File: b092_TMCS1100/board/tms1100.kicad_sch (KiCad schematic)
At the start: 5 parts, among them U1 TMCS1100

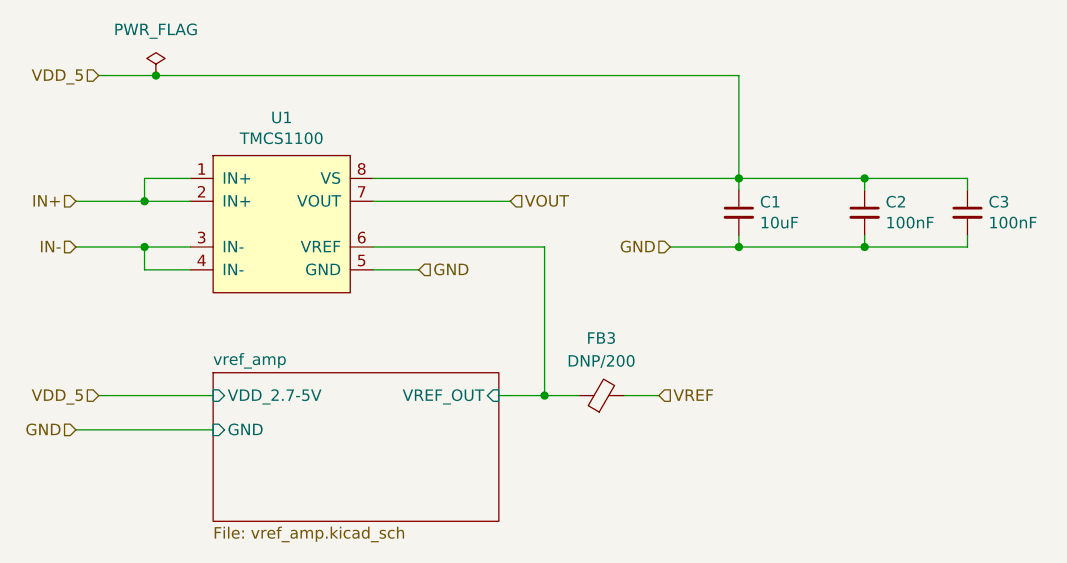
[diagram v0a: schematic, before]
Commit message: Update ref. voltage connections and fix via sizes
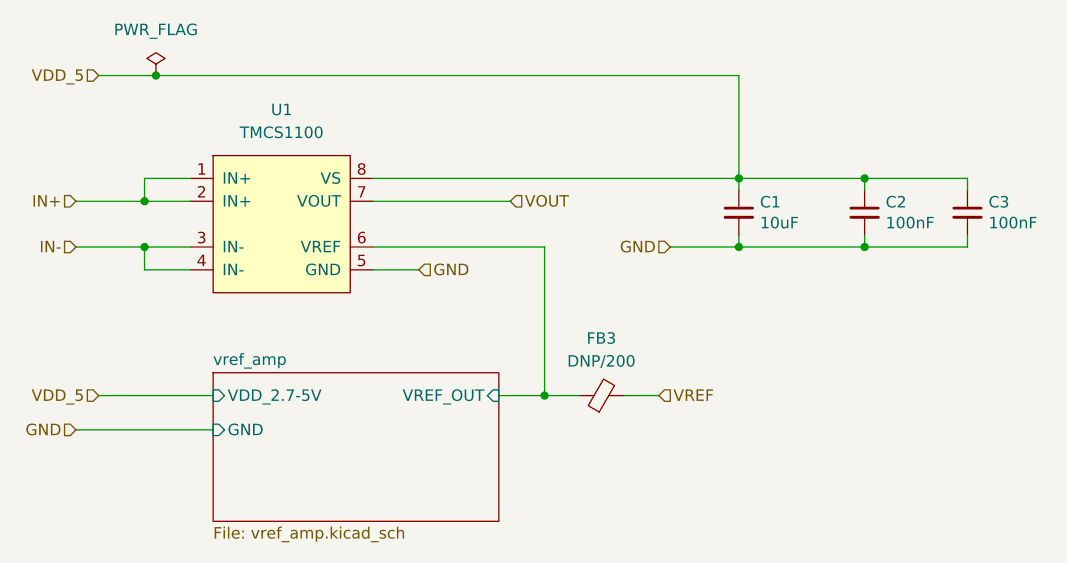
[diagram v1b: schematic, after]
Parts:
- removed U1: TMCS1100, 2021_bt5_headtracker_footprints:SOIC-8_5.4, symbol iso_curr_sns_TCMS1100-rescue:TMCS1100-2021_bt5_headtracker_symbols
- added U1: TMCS1100, AI-footprints:SOIC-8_5.4, symbol Auto-Intern:TMCS1100
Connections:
- net GND: now also U1.5 (GND)
- net IN+: now also U1.1 (IN+), U1.2 (IN+)
- net IN-: now also U1.3 (IN-), U1.4 (IN-)
- net VDD_5: now also U1.8 (VS)
- net VOUT: now also U1.7 (VOUT)
- net vref_amp/VREF_OUT: now also U1.6 (VREF)
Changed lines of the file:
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@@
     (pin "2")
-  )
-  (symbol (lib_id "iso_curr_sns_TCMS1100-rescue:TMCS1100-2021_bt5_headtracker_symbols") (at 132.08 102.87 0) (unit 1)
-    (in_bom yes) (on_board yes)
-    (property "Reference" "U1" (id 0) (at 132.08 91.059 0))
-    (property "Value" "TMCS1100" (id 1) (at 132.08 93.3704 0))
-    (property "Footprint" "2021_bt5_headtracker_footprints:SOIC-8_5.4" (id 2) (at 130.81 102.87 0)
-      (effects (font (size 1.27 1.27)) hide)
-    )
-    (property "Datasheet" "https://www.ti.com/lit/ds/symlink/tmcs1100.pdf?ts=1615404625916&ref_url=https%253A%252F%252Fwww.ti.com%252F" (id 3) (at 130.81 102.87 0)
-      (effects (font (size 1.27 1.27)) hide)
-    )
-    (pin "1")
-    (pin "2")
-    (pin "3")
-    (pin "4")
-    (pin "5")
-    (pin "6")
-    (pin "7")
-    (pin "8")
   )
   (symbol (lib_id "Device:C_Small") (at 196.85 101.6 0) (unit 1)
@@
     (pin "2")
   )
+  (symbol (lib_id "Auto-Intern:TMCS1100") (at 132.08 102.87 0) (unit 1)
+    (in_bom yes) (on_board yes) (fields_autoplaced)
+    (property "Reference" "U1" (id 0) (at 132.08 90.17 0))
+    (property "Value" "TMCS1100" (id 1) (at 132.08 92.71 0))
+    (property "Footprint" "AI-footprints:SOIC-8_5.4" (id 2) (at 130.81 102.87 0)
+      (effects (font (size 1.27 1.27)) hide)
+    )
+    (property "Datasheet" "https://www.ti.com/lit/ds/symlink/tmcs1100.pdf?ts=1615404625916&ref_url=https%253A%252F%252Fwww.ti.com%252F" (id 3) (at 130.81 102.87 0)
+      (effects (font (size 1.27 1.27)) hide)
+    )
+    (pin "1")
+    (pin "2")
+    (pin "3")
+    (pin "4")
+    (pin "5")
+    (pin "6")
+    (pin "7")
+    (pin "8")
+  )
   (sheet (at 124.46 119.38) (size 31.75 16.51) (fields_autoplaced)
